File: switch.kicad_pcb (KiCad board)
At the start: 2 copper layers, 50.8 x 50.8 mm, 6 parts, among them IC4 MM5230-03NDB-TR, J1 Conn_01x02, J2 Conn_Coaxial, J4 Conn_Coaxial, J7 Conn_01x02

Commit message: small tweaks on standards boards
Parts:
- moved J7 19.8 mm to (166.5, 115.2)
- moved J4 15.2 mm to (180.4, 125.4)
- moved J1 14.5 mm to (169.1, 135.6)
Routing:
- net Net-(IC4-RF4GATE): track 29.6 -> 10.2 mm
- net Net-(IC4-RF3GATE): track 29.6 -> 10.2 mm
- net Net-(IC4-RF2GATE): track 7.78 -> 11.0 mm
- net Net-(IC4-RF1GATE): track 7.76 -> 10.2 mm
- net GND: vias 191 -> 132
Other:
- board size 50.8 x 50.8 mm -> 35.6 x 25.4 mm

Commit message: updated SMA launch to SW microwave on all boards
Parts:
- J2, J4: footprint Connector_Coaxial:SMA_Molex_73251-1153_EdgeMount_Horizontal -> southwest-microwave-connectors:southwest-super-SMA-292-04A-12
- moved J4 5.18 mm to (185.6, 125.4)
- moved J2 4.92 mm to (150.0, 125.4)

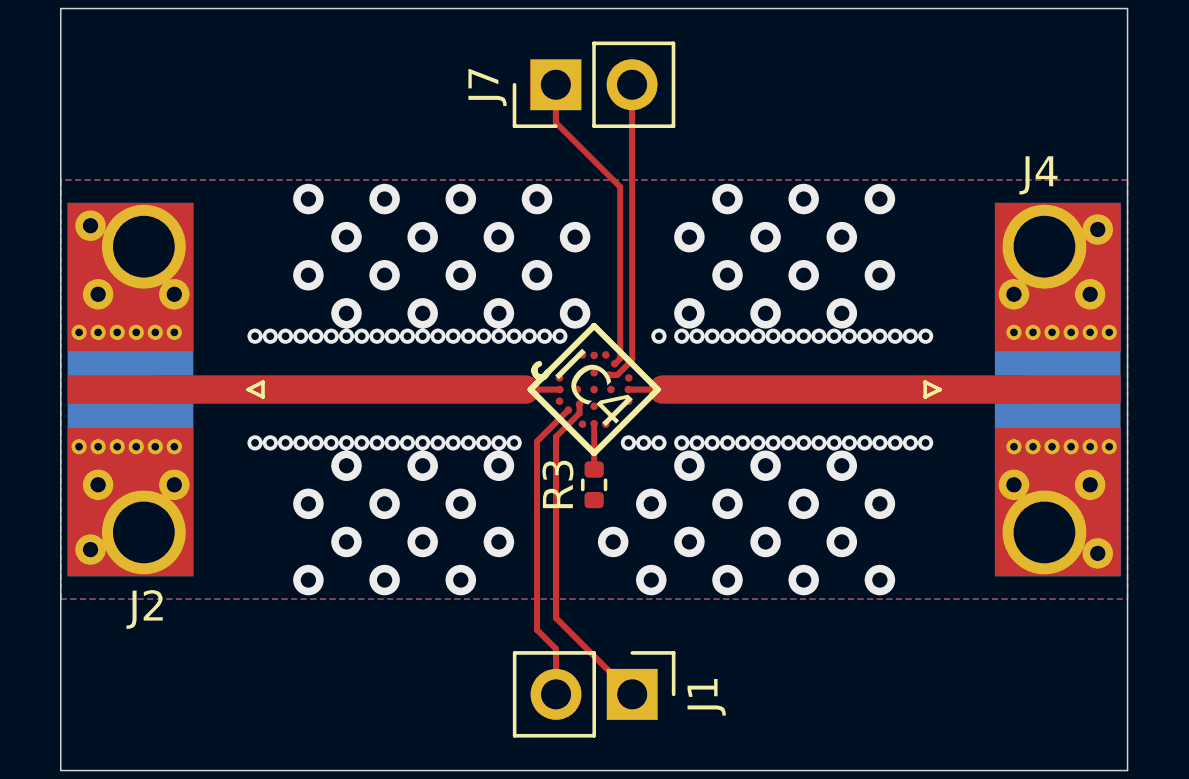
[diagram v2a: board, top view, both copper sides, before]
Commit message: used altium files to build kicad models of mm5800 and started new twpatron
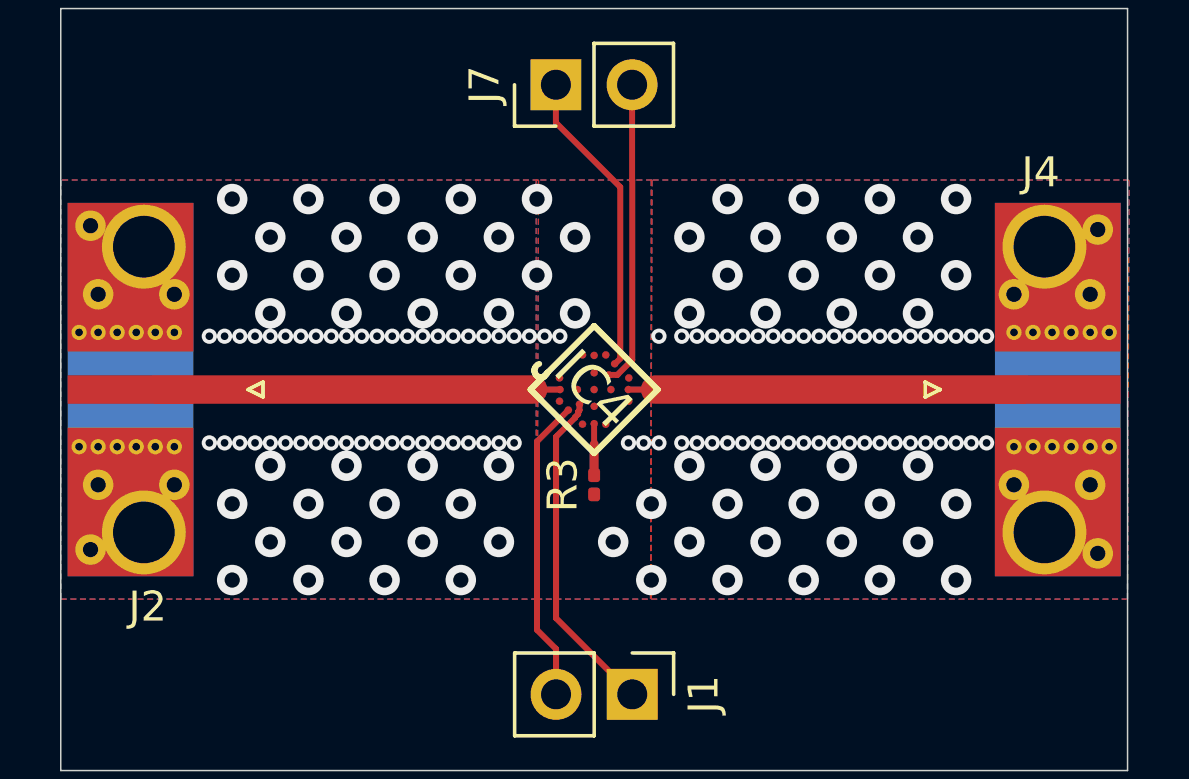
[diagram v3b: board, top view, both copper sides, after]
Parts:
- R3: footprint Resistor_SMD:R_0402_1005Metric -> Resistor_SMD:R_0201_0603Metric
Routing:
- net GND: vias 132 -> 162
